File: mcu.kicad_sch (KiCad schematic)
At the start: 12 parts, among them J3 Conn_01x04_Pin, SW31 SW_Push, U2 STM32L053C8T6

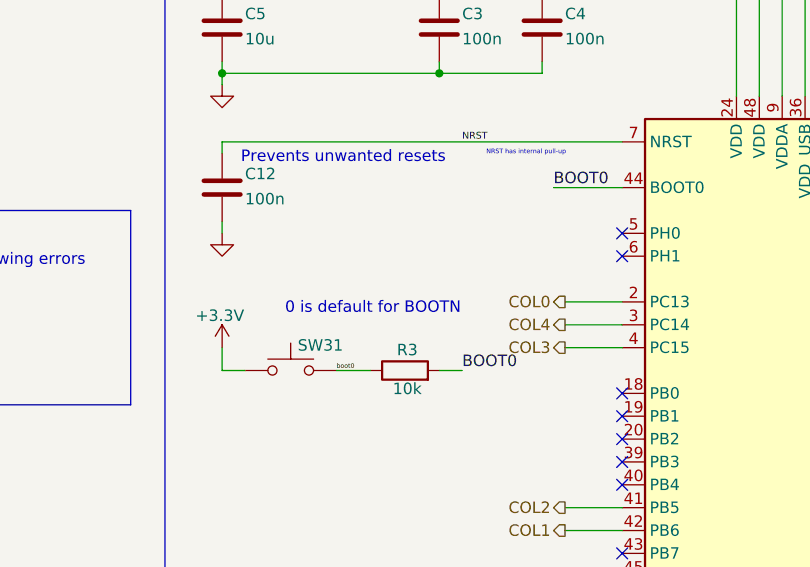
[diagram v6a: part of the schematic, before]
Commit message: added ESD protection, re-wired matrix
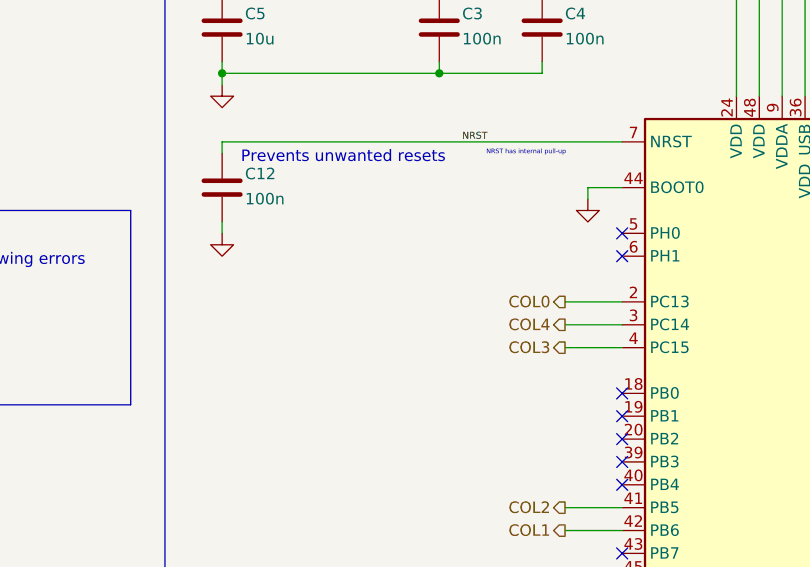
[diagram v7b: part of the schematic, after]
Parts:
- removed R3: 10k, Resistor_SMD:R_0402_1005Metric, symbol Device:R
- removed SW31: SW_Push, Diode_SMD:D_0805_2012Metric, symbol Switch:SW_Push
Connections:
- net BOOT0 is gone; now on net GND: U2.44 (BOOT0)
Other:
- note removed: "0 is default for BOOTN"
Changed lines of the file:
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@@
-	(wire
-		(pts
-			(xy 91.44 97.79) (xy 91.44 100.33)
-		)
-		(stroke
-			(width 0)
-			(type default)
-		)
-	)
 	(wire
 		(pts
@@
 	(wire
 		(pts
+			(xy 132.08 80.01) (xy 132.08 81.28)
+		)
+		(stroke
+			(width 0)
+			(type default)
+		)
+	)
+	(wire
+		(pts
 			(xy 185.42 34.29) (xy 185.42 35.56)
 		)
@@
 	(wire
 		(pts
-			(xy 128.27 80.01) (xy 135.89 80.01)
-		)
-		(stroke
-			(width 0)
-			(type default)
-		)
-	)
-	(wire
-		(pts
 			(xy 105.41 146.05) (xy 105.41 147.32)
 		)
@@
 	(wire
 		(pts
+			(xy 132.08 80.01) (xy 135.89 80.01)
+		)
+		(stroke
+			(width 0)
+			(type default)
+		)
+	)
+	(wire
+		(pts
 			(xy 153.67 148.59) (xy 153.67 151.13)
 		)
@@
 	(wire
 		(pts
-			(xy 115.57 100.33) (xy 118.11 100.33)
-		)
-		(stroke
-			(width 0)
-			(type default)
-		)
-	)
-	(wire
-		(pts
 			(xy 168.91 102.87) (xy 181.61 102.87)
 		)
@@
 	(wire
 		(pts
-			(xy 91.44 100.33) (xy 93.98 100.33)
-		)
-		(stroke
-			(width 0)
-			(type default)
-		)
-	)
-	(wire
-		(pts
 			(xy 185.42 66.04) (xy 185.42 67.31)
 		)
@@
 		(pts
 			(xy 91.44 54.61) (xy 91.44 57.15)
-		)
-		(stroke
-			(width 0)
-			(type default)
-		)
-	)
-	(wire
-		(pts
-			(xy 104.14 100.33) (xy 107.95 100.33)
 		)
 		(stroke
@@
 		)
 	)
-	(text "0 is default for BOOTN"
-		(exclude_from_sim no)
-		(at 108.204 93.472 0)
-		(effects
-			(font
-				(size 1.27 1.27)
-			)
-		)
-	)
 	(text "NRST has internal pull-up"
 		(exclude_from_sim no)
@@
 				(size 2.54 2.54)
 			)
-		)
-	)
-	(label "BOOT0"
-		(at 128.27 80.01 0)
-		(fields_autoplaced yes)
-		(effects
-			(font
-				(size 1.27 1.27)
-			)
-			(justify left bottom)
 		)
 	)
@@
 		)
 	)
-	(label "boot0"
-		(at 104.14 100.33 0)
-		(fields_autoplaced yes)
-		(effects
-			(font
-				(size 0.508 0.508)
-			)
-			(justify left bottom)
-		)
-	)
 	(label "SWCLK"
 		(at 172.72 110.49 0)
@@
 	(label "SWDIO"
 		(at 172.72 107.95 0)
-		(fields_autoplaced yes)
-		(effects
-			(font
-				(size 1.27 1.27)
-			)
-			(justify left bottom)
-		)
-	)
-	(label "BOOT0"
-		(at 118.11 100.33 0)
 		(fields_autoplaced yes)
 		(effects
@@
 	)
 	(symbol
-		(lib_id "Device:R")
-		(at 111.76 100.33 90)
-		(unit 1)
-		(exclude_from_sim no)
-		(in_bom yes)
-		(on_board yes)
-		(dnp no)
-		(property "Reference" "R3"
-			(at 112.014 98.044 90)
-			(effects
-				(font
-					(size 1.27 1.27)
-				)
-			)
-		)
-		(property "Value" "10k"
-			(at 112.014 102.362 90)
-			(effects
-				(font
-					(size 1.27 1.27)
-				)
-			)
-		)
-		(property "Footprint" "Resistor_SMD:R_0402_1005Metric"
-			(at 111.76 102.108 90)
-			(effects
-				(font
-					(size 1.27 1.27)
-				)
-				(hide yes)
-			)
-		)
-		(property "Datasheet" " ERJ-U2RD1002X"
-			(at 111.76 100.33 0)
-			(effects
-				(font
-					(size 1.27 1.27)
-				)
-				(hide yes)
-			)
-		)
-		(property "Description" "Resistor"
-			(at 111.76 100.33 0)
-			(effects
-				(font
-					(size 1.27 1.27)
-				)
-				(hide yes)
-			)
-		)
-		(pin "2"
-		)
-		(pin "1"
-		)
-		(instances
-			(project "stm_skeyboard"
-				(path "/f8cbad95-1fac-4ee0-b4c1-fc27b4678331/e572aac2-7f29-4ffb-8a77-de1db0d84645"
-					(reference "R3")
-					(unit 1)
-				)
-			)
-		)
-	)
-	(symbol
 		(lib_id "power:+3.3V")
 		(at 91.44 54.61 0)
@@
 	)
 	(symbol
-		(lib_id "Switch:SW_Push")
-		(at 99.06 100.33 0)
+		(lib_id "power:GND")
+		(at 132.08 81.28 0)
 		(unit 1)
 		(exclude_from_sim no)
@@
 		(on_board yes)
 		(dnp no)
-		(property "Reference" "SW31"
-			(at 102.362 97.536 0)
-			(effects
-				(font
-					(size 1.27 1.27)
-				)
-			)
-		)
-		(property "Value" "SW_Push"
-			(at 99.06 95.25 0)
-			(effects
-				(font
-					(size 1.27 1.27)
-				)
-				(hide yes)
-			)
-		)
-		(property "Footprint" "Diode_SMD:D_0805_2012Metric"
-			(at 99.06 95.25 0)
-			(effects
-				(font
-					(size 1.27 1.27)
-				)
-				(hide yes)
-			)
-		)
-		(property "Datasheet" "~"
-			(at 99.06 95.25 0)
-			(effects
-				(font
-					(size 1.27 1.27)
-				)
-				(hide yes)
-			)
-		)
-		(property "Description" "Push button switch, generic, two pins"
-			(at 99.06 100.33 0)
+		(fields_autoplaced yes)
+		(property "Reference" "#PWR01"
+			(at 132.08 87.63 0)
+			(effects
+				(font
+					(size 1.27 1.27)
+				)
+				(hide yes)
+			)
+		)
+		(property "Value" "GND"
+			(at 132.08 86.36 0)
+			(effects
+				(font
+					(size 1.27 1.27)
+				)
+				(hide yes)
+			)
+		)
+		(property "Footprint" ""
+			(at 132.08 81.28 0)
+			(effects
+				(font
+					(size 1.27 1.27)
+				)
+				(hide yes)
+			)
+		)
+		(property "Datasheet" ""
+			(at 132.08 81.28 0)
+			(effects
+				(font
+					(size 1.27 1.27)
+				)
+				(hide yes)
+			)
+		)
+		(property "Description" "Power symbol creates a global label with name \"GND\" , ground"
+			(at 132.08 81.28 0)
 			(effects
 				(font
@@
 		)
 		(pin "1"
-		)
-		(pin "2"
 		)
 		(instances
 			(project "stm_skeyboard"
 				(path "/f8cbad95-1fac-4ee0-b4c1-fc27b4678331/e572aac2-7f29-4ffb-8a77-de1db0d84645"
-					(reference "SW31")
+					(reference "#PWR01")
 					(unit 1)
 				)
@@
 					(unit 1)
 				)
-			)
-		)
-	)
-	(symbol
-		(lib_id "power:+3.3V")
-		(at 91.44 97.79 0)
-		(unit 1)
-		(exclude_from_sim no)
-		(in_bom yes)
-		(on_board yes)
-		(dnp no)
-		(property "Reference" "#PWR0104"
-			(at 91.44 101.6 0)
-			(effects
-				(font
-					(size 1.27 1.27)
-				)
-				(hide yes)
-			)
-		)
-		(property "Value" "+3.3V"
-			(at 91.186 94.234 0)
-			(effects
-				(font
-					(size 1.27 1.27)
-				)
-			)
-		)
-		(property "Footprint" ""
-			(at 91.44 97.79 0)
-			(effects
-				(font
-					(size 1.27 1.27)
-				)
-				(hide yes)
-			)
-		)
-		(property "Datasheet" ""
-			(at 91.44 97.79 0)
-			(effects
-				(font
-					(size 1.27 1.27)
-				)
-				(hide yes)
-			)
-		)
-		(property "Description" "Power symbol creates a global label with name \"+3.3V\""
-			(at 91.44 97.79 0)
-			(effects
-				(font
-					(size 1.27 1.27)
-				)
-				(hide yes)
-			)
-		)
-		(pin "1"
-		)
-		(instances
-			(project "stm_skeyboard"
-				(path "/f8cbad95-1fac-4ee0-b4c1-fc27b4678331/e572aac2-7f29-4ffb-8a77-de1db0d84645"
-					(reference "#PWR0104")
-					(unit 1)
-				)
